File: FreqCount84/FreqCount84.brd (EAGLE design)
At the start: 160 x 100 mm, 63 parts, among them IC1 74LS595D, IC2 74LS595D, IC3 74LS595D, IC4 74S151D, IC5 7805T, IC6 74AHCU04, Q1 20.000MHz, T1 2N3904

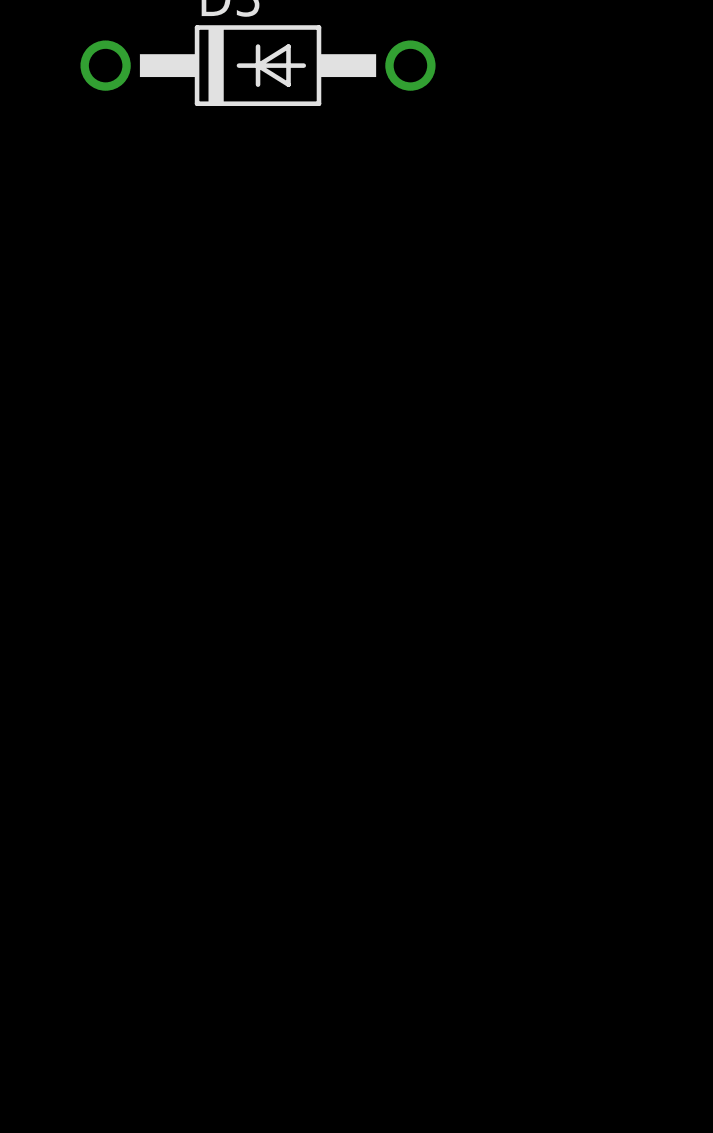
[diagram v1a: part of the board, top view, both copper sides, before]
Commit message: added the FTDI USB->RS232 chip into the schematic because I am using it now.
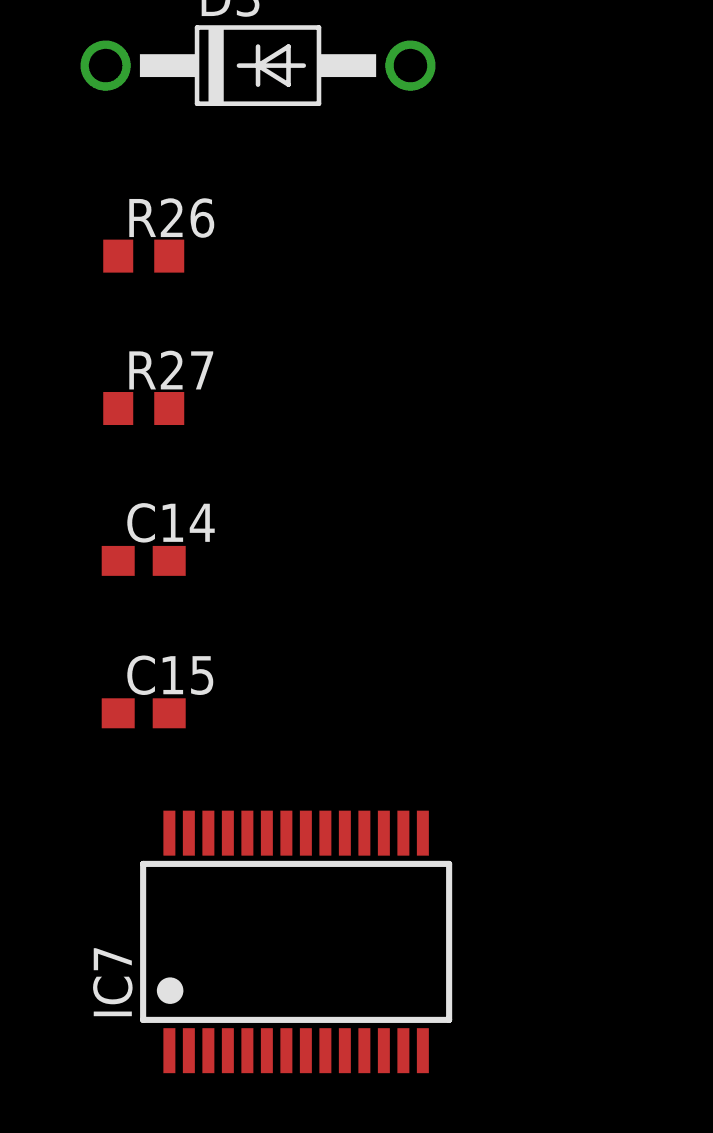
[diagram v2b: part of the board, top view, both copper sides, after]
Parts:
- added C14, C15: 100p, rcl:C0603
- added IC7: FT232RL, ftdichip:SSOP28
- added R26, R27: 470, rcl:R0603
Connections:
- removed net N$44 (its old number): IC6.4, IC6.5
- new net N$23: C15.2, IC6.3, R26.2
- new net N$42: C14.2, IC6.13, R27.2
- new net N$51: IC6.10
- new net N$53: IC7.1, U$1.13
- new net N$58: IC7.15
- new net N$59: IC7.16
- new net N$60: IC7.20
- new net VCCIO: IC7.4
- net +5V: now also IC6.5
- net GND: now also C14.1, C15.1, IC7.18, IC7.21, IC7.25, IC7.7
- net N$22: now also R26.1; no longer IC6.3
- net N$43: now also IC6.4, R27.1; no longer IC6.10, IC6.13
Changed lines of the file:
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@@
 <element name="D2" library="diode" package="DO41-10" value="1N4004" x="-77.47" y="-293.37"/>
 <element name="D3" library="diode" package="DO41-10" value="1N4004" x="-77.47" y="-300.99"/>
+<element name="R26" library="rcl" package="R0603" value="470" x="-81.28" y="-307.34"/>
+<element name="R27" library="rcl" package="R0603" value="470" x="-81.28" y="-312.42"/>
+<element name="C14" library="rcl" package="C0603" value="100p" x="-81.28" y="-317.5"/>
+<element name="C15" library="rcl" package="C0603" value="100p" x="-81.28" y="-322.58"/>
+<element name="IC7" library="ftdichip" package="SSOP28" value="FT232RL" x="-76.2" y="-330.2">
+<attribute name="OC_NEWARK" value="91K9918" x="-76.2" y="-330.2" size="1.778" layer="27" display="off"/>
+<attribute name="MPN" value="FT232RL" x="-76.2" y="-330.2" size="1.778" layer="27" display="off"/>
+<attribute name="MF" value="" x="-76.2" y="-330.2" size="1.778" layer="27" display="off"/>
+<attribute name="OC_FARNELL" value="1146032" x="-76.2" y="-330.2" size="1.778" layer="27" display="off"/>
+</element>
 </elements>
 <signals>
@@
 <contactref element="IC5" pad="2"/>
 <contactref element="JP1" pad="6"/>
-<contactref element="U$1" pad="14"/>
 <contactref element="IC2" pad="8"/>
 <contactref element="IC3" pad="8"/>
@@
 <contactref element="C1" pad="2"/>
 <contactref element="C11" pad="1"/>
-<contactref element="C2" pad="2"/>
 <contactref element="IC4" pad="8"/>
 <contactref element="IC4" pad="7"/>
@@
 <contactref element="D1" pad="A"/>
 <contactref element="D2" pad="A"/>
+<contactref element="C15" pad="1"/>
+<contactref element="C14" pad="1"/>
+<contactref element="IC7" pad="25"/>
+<contactref element="U$1" pad="14"/>
+<contactref element="C2" pad="2"/>
+<contactref element="IC7" pad="21"/>
+<contactref element="IC7" pad="18"/>
+<contactref element="IC7" pad="7"/>
 <wire x1="-71.755" y1="-191.0334" x2="-67.73" y2="-186.69" width="0" layer="19" extent="1-1"/>
 <wire x1="-73.025" y1="-191.0334" x2="-71.755" y2="-191.0334" width="0" layer="19" extent="1-1"/>
@@
 <wire x1="-72.39" y1="-285.75" x2="-82.55" y2="-257.81" width="0" layer="19" extent="1-1"/>
 <wire x1="-72.39" y1="-293.37" x2="-72.39" y2="-285.75" width="0" layer="19" extent="1-1"/>
+<wire x1="-82.13" y1="-317.5" x2="-72.39" y2="-293.37" width="0" layer="19" extent="1-1"/>
+<wire x1="-82.13" y1="-322.58" x2="-82.13" y2="-317.5" width="0" layer="19" extent="1-1"/>
+<wire x1="-78.475" y1="-326.575" x2="-82.13" y2="-322.58" width="0" layer="19" extent="1-1"/>
+<wire x1="-75.875" y1="-326.575" x2="-78.475" y2="-326.575" width="0" layer="19" extent="1-1"/>
+<wire x1="-73.925" y1="-326.575" x2="-75.875" y2="-326.575" width="0" layer="19" extent="1-1"/>
+<wire x1="-76.525" y1="-333.825" x2="-75.875" y2="-326.575" width="0" layer="19" extent="1-1"/>
 <wire x1="-82.55" y1="-101.6" x2="-82.13" y2="-168.91" width="0" layer="19" extent="1-1"/>
 <wire x1="-82.55" y1="-95.25" x2="-82.55" y2="-101.6" width="0" layer="19" extent="1-1"/>
@@
 <contactref element="R22" pad="1"/>
 <contactref element="D3" pad="C"/>
+<contactref element="IC6" pad="5"/>
 <wire x1="-82.13" y1="-269.24" x2="-82.55" y2="-300.99" width="0" layer="19" extent="1-1"/>
 <wire x1="-82.13" y1="-264.16" x2="-82.13" y2="-269.24" width="0" layer="19" extent="1-1"/>
 <wire x1="-80.43" y1="-215.9" x2="-82.13" y2="-264.16" width="0" layer="19" extent="1-1"/>
-<wire x1="-75.35" y1="-195.58" x2="-80.43" y2="-215.9" width="0" layer="19" extent="1-1"/>
+<wire x1="-76.2" y1="-206.2734" x2="-80.43" y2="-215.9" width="0" layer="19" extent="1-1"/>
+<wire x1="-75.35" y1="-195.58" x2="-76.2" y2="-206.2734" width="0" layer="19" extent="1-1"/>
 <wire x1="-70.27" y1="-195.58" x2="-75.35" y2="-195.58" width="0" layer="19" extent="1-1"/>
 <wire x1="-80.43" y1="-40.64" x2="-75.35" y2="-195.58" width="0" layer="19" extent="1-1"/>
@@
 <signal name="N$22">
 <contactref element="IC6" pad="2"/>
-<contactref element="IC6" pad="3"/>
 <contactref element="R3" pad="2"/>
+<contactref element="R26" pad="1"/>
+<wire x1="-80.43" y1="-226.06" x2="-82.13" y2="-307.34" width="0" layer="19" extent="1-1"/>
 <wire x1="-80.01" y1="-206.2734" x2="-80.43" y2="-226.06" width="0" layer="19" extent="1-1"/>
-<wire x1="-78.74" y1="-206.2734" x2="-80.01" y2="-206.2734" width="0" layer="19" extent="1-1"/>
-</signal>
-<signal name="N$23">
-<contactref element="IC6" pad="6"/>
-<contactref element="IC6" pad="9"/>
-<wire x1="-74.93" y1="-200.1266" x2="-74.93" y2="-206.2734" width="0" layer="19" extent="1-1"/>
-</signal>
-<signal name="N$42">
-<contactref element="IC6" pad="8"/>
-<contactref element="IC6" pad="11"/>
-<wire x1="-73.66" y1="-200.1266" x2="-77.47" y2="-200.1266" width="0" layer="19" extent="1-1"/>
-</signal>
-<signal name="N$43">
-<contactref element="IC6" pad="10"/>
-<contactref element="IC6" pad="13"/>
-<wire x1="-76.2" y1="-200.1266" x2="-80.01" y2="-200.1266" width="0" layer="19" extent="1-1"/>
-</signal>
-<signal name="N$44">
-<contactref element="IC6" pad="4"/>
-<contactref element="IC6" pad="5"/>
-<wire x1="-76.2" y1="-206.2734" x2="-77.47" y2="-206.2734" width="0" layer="19" extent="1-1"/>
 </signal>
 <signal name="N$45">
@@
 <wire x1="-81.7372" y1="-231.1908" x2="-80.43" y2="-279.4" width="0" layer="19" extent="1-1"/>
 </signal>
+<signal name="N$23">
+<contactref element="R26" pad="2"/>
+<contactref element="IC6" pad="3"/>
+<contactref element="C15" pad="2"/>
+<wire x1="-80.43" y1="-307.34" x2="-80.43" y2="-322.58" width="0" layer="19" extent="1-1"/>
+<wire x1="-78.74" y1="-206.2734" x2="-80.43" y2="-307.34" width="0" layer="19" extent="1-1"/>
+</signal>
+<signal name="N$42">
+<contactref element="IC6" pad="13"/>
+<contactref element="R27" pad="2"/>
+<contactref element="C14" pad="2"/>
+<wire x1="-80.43" y1="-312.42" x2="-80.43" y2="-317.5" width="0" layer="19" extent="1-1"/>
+<wire x1="-80.01" y1="-200.1266" x2="-80.43" y2="-312.42" width="0" layer="19" extent="1-1"/>
+</signal>
+<signal name="N$43">
+<contactref element="R27" pad="1"/>
+<contactref element="IC6" pad="4"/>
+<wire x1="-77.47" y1="-206.2734" x2="-82.13" y2="-312.42" width="0" layer="19" extent="1-1"/>
+</signal>
+<signal name="N$44">
+<contactref element="IC6" pad="9"/>
+<contactref element="IC6" pad="6"/>
+<wire x1="-74.93" y1="-200.1266" x2="-74.93" y2="-206.2734" width="0" layer="19" extent="1-1"/>
+</signal>
+<signal name="N$48">
+<contactref element="IC6" pad="11"/>
+<contactref element="IC6" pad="8"/>
+<wire x1="-73.66" y1="-200.1266" x2="-77.47" y2="-200.1266" width="0" layer="19" extent="1-1"/>
+</signal>
+<signal name="N$51">
+<contactref element="IC6" pad="10"/>
+</signal>
+<signal name="VCCIO">
+<contactref element="IC7" pad="4"/>
+</signal>
+<signal name="N$53">
+<contactref element="IC7" pad="1"/>
+<contactref element="U$1" pad="13"/>
+<wire x1="-68.58" y1="41.1734" x2="-80.425" y2="-333.825" width="0" layer="19" extent="1-1"/>
+</signal>
+<signal name="N$58">
+<contactref element="IC7" pad="15"/>
+</signal>
+<signal name="N$59">
+<contactref element="IC7" pad="16"/>
+</signal>
+<signal name="N$60">
+<contactref element="IC7" pad="20"/>
+</signal>
 </signals>

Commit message: adding notes to FTDI RS232 chip.
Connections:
- new net N$55: IC7.5, U$1.12
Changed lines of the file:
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@@
 <contactref element="IC7" pad="20"/>
+</signal>
+<signal name="N$55">
+<contactref element="IC7" pad="5"/>
+<contactref element="U$1" pad="12"/>
+<wire x1="-67.31" y1="41.1734" x2="-77.825" y2="-333.825" width="0" layer="19" extent="1-1"/>
 </signal>
 </signals>
